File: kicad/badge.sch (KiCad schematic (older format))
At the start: 11 parts, among them SW1 SPST

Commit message: wire pin 20 and 21 to +5v
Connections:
- net +5V: now also IC?.20 (AVCC), IC?.21 (AREF)
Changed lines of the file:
@@
 	8200 2650 8200 3150
 Connection ~ 8200 3150
+Wire Wire Line
+	4550 2650 4550 3250
+Wire Wire Line
+	4550 3250 4700 3250
+Connection ~ 4550 2650
+Wire Wire Line
+	4700 2950 4550 2950
+Connection ~ 4550 2950
 $EndSCHEMATC

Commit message: 9v battery connector
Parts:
- added P?: 9v battery, symbol CONN_01X02
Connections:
- net GND: now also P?.1 (P1)
- net VCC: now also P?.2 (P2)
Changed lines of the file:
@@
 	4700 2950 4550 2950
 Connection ~ 4550 2950
+$Comp
+L CONN_01X02 P?
+U 1 1 58E1B172
+P 2450 1000
+F 0 "P?" H 2450 1150 50  0000 C CNN
+F 1 "9v battery " V 2550 1000 50  0000 C CNN
+F 2 "" H 2450 1000 50  0000 C CNN
+F 3 "" H 2450 1000 50  0000 C CNN
+	1    2450 1000
+	-1   0    0    1
+$EndComp
+$Comp
+L VCC #PWR?
+U 1 1 58E1B2A6
+P 3000 900
+F 0 "#PWR?" H 3000 750 50  0001 C CNN
+F 1 "VCC" H 3000 1050 50  0000 C CNN
+F 2 "" H 3000 900 50  0000 C CNN
+F 3 "" H 3000 900 50  0000 C CNN
+	1    3000 900
+	1    0    0    -1
+$EndComp
+$Comp
+L GND #PWR?
+U 1 1 58E1B2D2
+P 3000 1200
+F 0 "#PWR?" H 3000 950 50  0001 C CNN
+F 1 "GND" H 3000 1050 50  0000 C CNN
+F 2 "" H 3000 1200 50  0000 C CNN
+F 3 "" H 3000 1200 50  0000 C CNN
+	1    3000 1200
+	1    0    0    -1
+$EndComp
+Wire Wire Line
+	2650 950  3000 950
+Wire Wire Line
+	3000 950  3000 900
+Wire Wire Line
+	2650 1050 3000 1050
+Wire Wire Line
+	3000 1050 3000 1200
 $EndSCHEMATC

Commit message: FTDI programmer connection pins
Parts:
- added P?: FTDI programmer, symbol CONN_01X06
- C?: value C -> 0.1uF
- C?: value C -> 0x33uF
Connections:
- net +5V: now also P?.5 (P5)
- net at IC?.1 ((PCINT14/~RESET~)PC6): now also P?.1 (P1)
- net at IC?.2 ((PCINT16/RXD)PD0): now also P?.2 (P2)
- net at IC?.3 ((PCINT17/TXD)PD1): now also P?.3 (P3)
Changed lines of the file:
@@
 P 2600 1950
 F 0 "C?" H 2625 2050 50  0000 L CNN
-F 1 "C" H 2625 1850 50  0000 L CNN
+F 1 "0.1uF" H 2625 1850 50  0000 L CNN
 F 2 "" H 2638 1800 50  0000 C CNN
 F 3 "" H 2600 1950 50  0000 C CNN
@@
 P 1300 2000
 F 0 "C?" H 1325 2100 50  0000 L CNN
-F 1 "C" H 1325 1900 50  0000 L CNN
+F 1 "0x33uF" H 1325 1900 50  0000 L CNN
 F 2 "" H 1338 1850 50  0000 C CNN
 F 3 "" H 1300 2000 50  0000 C CNN
@@
 Wire Wire Line
 	3000 1050 3000 1200
+$Comp
+L CONN_01X06 P?
+U 1 1 58E1B8C9
+P 7550 4350
+F 0 "P?" H 7550 4700 50  0000 C CNN
+F 1 "FTDI programmer" V 7650 4350 50  0000 C CNN
+F 2 "" H 7550 4350 50  0000 C CNN
+F 3 "" H 7550 4350 50  0000 C CNN
+	1    7550 4350
+	1    0    0    -1
+$EndComp
+$Comp
+L GND #PWR?
+U 1 1 58E1B9A0
+P 7250 4750
+F 0 "#PWR?" H 7250 4500 50  0001 C CNN
+F 1 "GND" H 7250 4600 50  0000 C CNN
+F 2 "" H 7250 4750 50  0000 C CNN
+F 3 "" H 7250 4750 50  0000 C CNN
+	1    7250 4750
+	1    0    0    -1
+$EndComp
+Wire Wire Line
+	7400 4600 7250 4600
+Wire Wire Line
+	7250 4600 7250 4750
+Wire Wire Line
+	6600 4100 7350 4100
+Wire Wire Line
+	6600 4250 6750 4250
+Wire Wire Line
+	6750 4250 6750 4200
+Wire Wire Line
+	6750 4200 7350 4200
+Wire Wire Line
+	6600 4350 7150 4350
+Wire Wire Line
+	7150 4350 7150 4300
+Wire Wire Line
+	7150 4300 7350 4300
+$Comp
+L +5V #PWR?
+U 1 1 58E1BF97
+P 7000 4750
+F 0 "#PWR?" H 7000 4600 50  0001 C CNN
+F 1 "+5V" H 7000 4890 50  0000 C CNN
+F 2 "" H 7000 4750 50  0000 C CNN
+F 3 "" H 7000 4750 50  0000 C CNN
+	1    7000 4750
+	-1   0    0    1
+$EndComp
+Wire Wire Line
+	7000 4500 7000 4750
+Wire Wire Line
+	7000 4500 7350 4500
 $EndSCHEMATC

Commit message: fix value and reference componentc fields
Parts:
- removed 16Mhz1: Crystal, symbol Crystal
- removed 22pF2: C, symbol C
- removed R1: R, symbol R
- added C?: 22pF, symbol C
- added Y?: 16Mhz, symbol Crystal
- C?: renamed from 22pF1; value C -> 22pF
- C?: renamed from 10uF1; value C -> 10uF
- R?: renamed from 10k1; value R -> 10k
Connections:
- net GND: now also C?.1
- net at C?.2, IC?.9 ((PCINT6/XTAL1/TOSC1)PB6): now also Y?.1
- net at IC?.10 ((PCINT7/XTAL2/TOSC2)PB7): now also C?.2, Y?.2
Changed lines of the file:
@@
 $EndDescr
-$Comp
-L R R1
-U 1 1 58E158FB
-P 6100 3850
-F 0 "R1" V 6180 3850 50  0000 C CNN
-F 1 "R" V 6100 3850 50  0000 C CNN
-F 2 "" V 6030 3850 50  0000 C CNN
-F 3 "" H 6100 3850 50  0000 C CNN
-	1    6100 3850
-	1    0    0    -1
-$EndComp
 $Comp
 L GND #PWR01
@@
 $EndComp
 $Comp
-L R 10k1
+L R R?
 U 1 1 58E15AC1
 P 7450 2250
-F 0 "10k1" V 7530 2250 50  0000 C CNN
-F 1 "R" V 7450 2250 50  0000 C CNN
+F 0 "R?" V 7530 2250 50  0000 C CNN
+F 1 "10k" V 7450 2250 50  0000 C CNN
 F 2 "" V 7380 2250 50  0000 C CNN
 F 3 "" H 7450 2250 50  0000 C CNN
@@
 $EndComp
 $Comp
-L Crystal 16Mhz1
-U 1 1 58E15B48
-P 7350 3350
-F 0 "16Mhz1" H 7350 3500 50  0000 C CNN
-F 1 "Crystal" H 7350 3200 50  0000 C CNN
-F 2 "" H 7350 3350 50  0000 C CNN
-F 3 "" H 7350 3350 50  0000 C CNN
-	1    7350 3350
-	0    1    1    0
-$EndComp
-$Comp
-L C 22pF1
+L C C?
 U 1 1 58E15B8A
 P 7700 3100
-F 0 "22pF1" H 7725 3200 50  0000 L CNN
-F 1 "C" H 7725 3000 50  0000 L CNN
+F 0 "C?" H 7725 3200 50  0000 L CNN
+F 1 "22pF" H 7725 3000 50  0000 L CNN
 F 2 "" H 7738 2950 50  0000 C CNN
 F 3 "" H 7700 3100 50  0000 C CNN
 	1    7700 3100
-	0    1    1    0
-$EndComp
-$Comp
-L C 22pF2
-U 1 1 58E15BB3
-P 7750 3650
-F 0 "22pF2" H 7775 3750 50  0000 L CNN
-F 1 "C" H 7775 3550 50  0000 L CNN
-F 2 "" H 7788 3500 50  0000 C CNN
-F 3 "" H 7750 3650 50  0000 C CNN
-	1    7750 3650
 	0    1    1    0
 $EndComp
@@
 $EndComp
 $Comp
-L C 10uF1
+L C C?
 U 1 1 58E164D8
 P 4150 2800
-F 0 "10uF1" H 4175 2900 50  0000 L CNN
-F 1 "C" H 4175 2700 50  0000 L CNN
+F 0 "C?" H 4175 2900 50  0000 L CNN
+F 1 "10uF" H 4175 2700 50  0000 L CNN
 F 2 "" H 4188 2650 50  0000 C CNN
 F 3 "" H 4150 2800 50  0000 C CNN
@@
 $EndComp
 Wire Wire Line
-	6800 3100 7550 3100
+	6800 3100 7350 3100
+Wire Wire Line
+	7350 3100 7550 3100
 Wire Wire Line
 	7350 3200 7350 3100
@@
 	7350 3500 7350 3650
 Wire Wire Line
-	6800 3650 7600 3650
+	6800 3650 7350 3650
+Wire Wire Line
+	7350 3650 7600 3650
 Wire Wire Line
 	7850 3100 8200 3100
 Wire Wire Line
-	8200 3100 8200 3800
+	8200 3100 8200 3150
+Wire Wire Line
+	8200 3150 8200 3650
+Wire Wire Line
+	8200 3650 8200 3800
 Wire Wire Line
 	7900 3650 8200 3650
@@
 	4700 4850 4450 4850
 Wire Wire Line
-	4150 2650 4700 2650
+	4150 2650 4550 2650
+Wire Wire Line
+	4550 2650 4700 2650
 Wire Wire Line
 	4150 2650 4150 2250
@@
 	4150 2950 4150 3100
 Wire Wire Line
-	6600 2650 6950 2650
+	6600 2650 6850 2650
+Wire Wire Line
+	6850 2650 6950 2650
 Wire Wire Line
 	7300 2250 6850 2250
@@
 	7900 2250 7600 2250
 Wire Wire Line
-	1300 1750 1600 1750
+	1300 1750 1500 1750
+Wire Wire Line
+	1500 1750 1600 1750
 Wire Wire Line
 	1300 1750 1300 1850
 Wire Wire Line
-	2000 2050 2000 2350
+	2000 2050 2000 2250
+Wire Wire Line
+	2000 2250 2000 2350
 Wire Wire Line
 	1300 2150 1300 2250
 Wire Wire Line
-	1300 2250 2600 2250
+	1300 2250 2000 2250
+Wire Wire Line
+	2000 2250 2600 2250
 Connection ~ 2000 2250
 Wire Wire Line
 	2600 2250 2600 2100
 Wire Wire Line
-	2400 1750 3100 1750
+	2400 1750 2600 1750
+Wire Wire Line
+	2600 1750 3100 1750
 Wire Wire Line
 	2600 1750 2600 1800
@@
 Connection ~ 7350 3650
 Wire Wire Line
-	4450 4850 4450 5150
+	4450 4850 4450 4950
+Wire Wire Line
+	4450 4950 4450 5150
 Wire Wire Line
 	7950 2650 8200 2650
@@
 Connection ~ 8200 3150
 Wire Wire Line
-	4550 2650 4550 3250
+	4550 2650 4550 2950
+Wire Wire Line
+	4550 2950 4550 3250
 Wire Wire Line
 	4550 3250 4700 3250
@@
 Wire Wire Line
 	7000 4500 7350 4500
+$Comp
+L Crystal Y?
+U 1 1 58E1C7EA
+P 7350 3350
+F 0 "Y?" H 7350 3500 50  0000 C CNN
+F 1 "16Mhz" H 7350 3200 50  0000 C CNN
+F 2 "" H 7350 3350 50  0000 C CNN
+F 3 "" H 7350 3350 50  0000 C CNN
+	1    7350 3350
+	0    1    1    0
+$EndComp
+$Comp
+L C C?
+U 1 1 58E1C898
+P 7750 3650
+F 0 "C?" H 7775 3750 50  0000 L CNN
+F 1 "22pF" H 7775 3550 50  0000 L CNN
+F 2 "" H 7788 3500 50  0000 C CNN
+F 3 "" H 7750 3650 50  0000 C CNN
+	1    7750 3650
+	0    1    1    0
+$EndComp
 $EndSCHEMATC

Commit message: fix value: 33uF -> 0.33uF
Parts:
- C?: value 0x33uF -> 0.33uF
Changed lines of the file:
@@
 P 1300 2000
 F 0 "C?" H 1325 2100 50  0000 L CNN
-F 1 "0x33uF" H 1325 1900 50  0000 L CNN
+F 1 "0.33uF" H 1325 1900 50  0000 L CNN
 F 2 "" H 1338 1850 50  0000 C CNN
 F 3 "" H 1300 2000 50  0000 C CNN

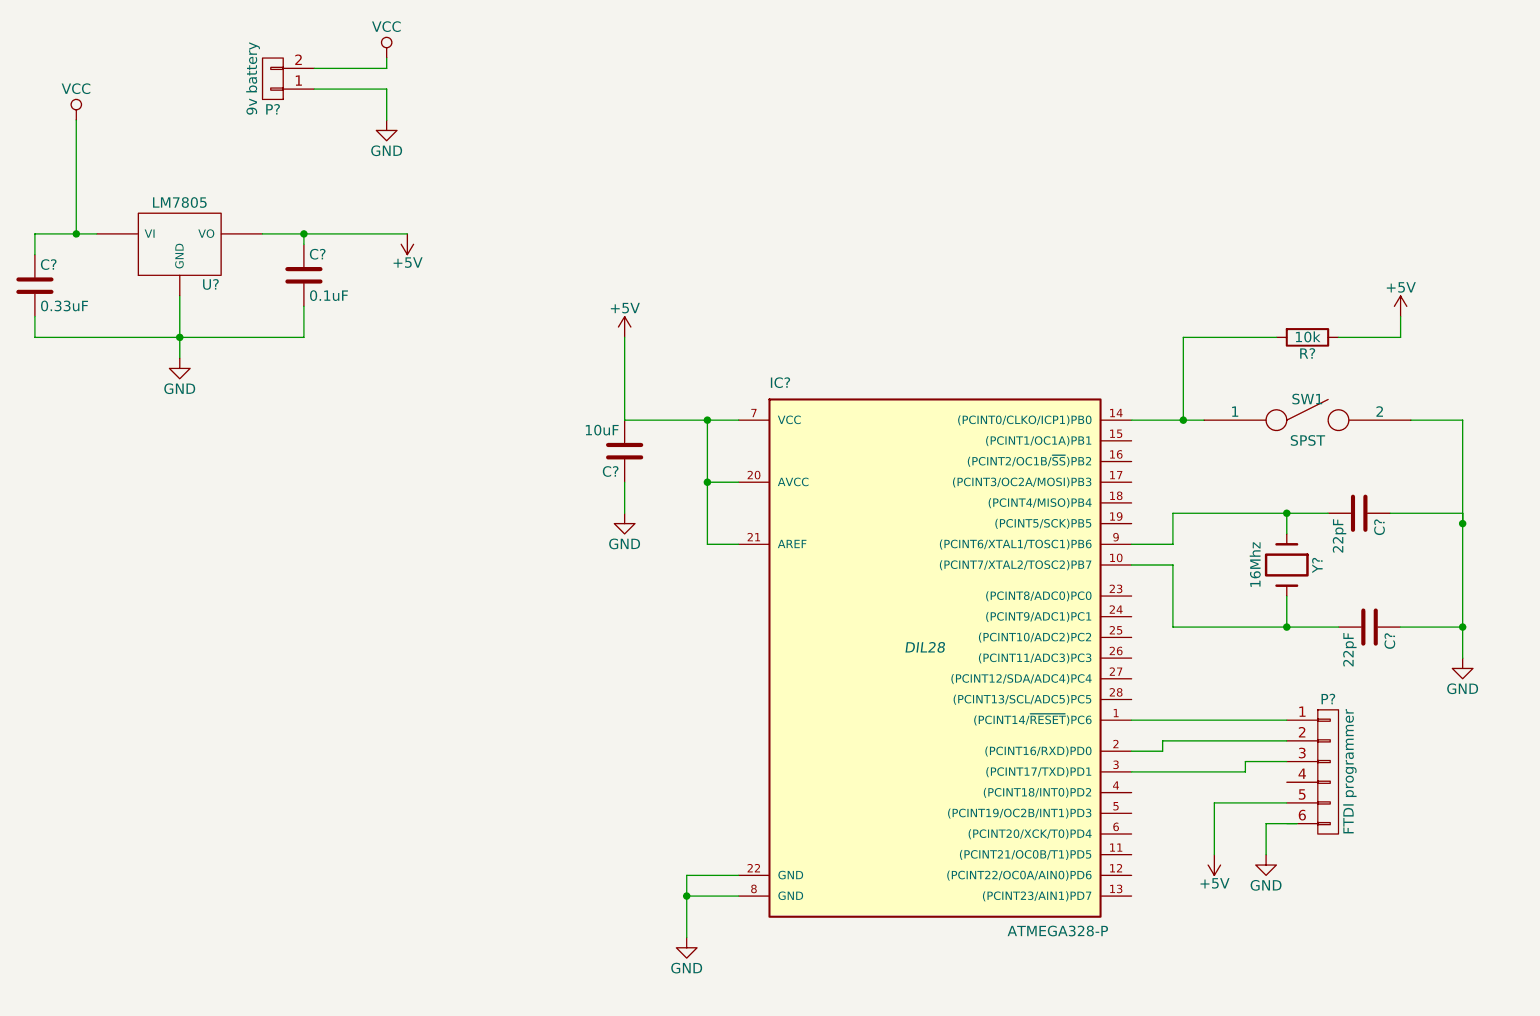
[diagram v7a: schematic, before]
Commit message: fix ftdi connector trace
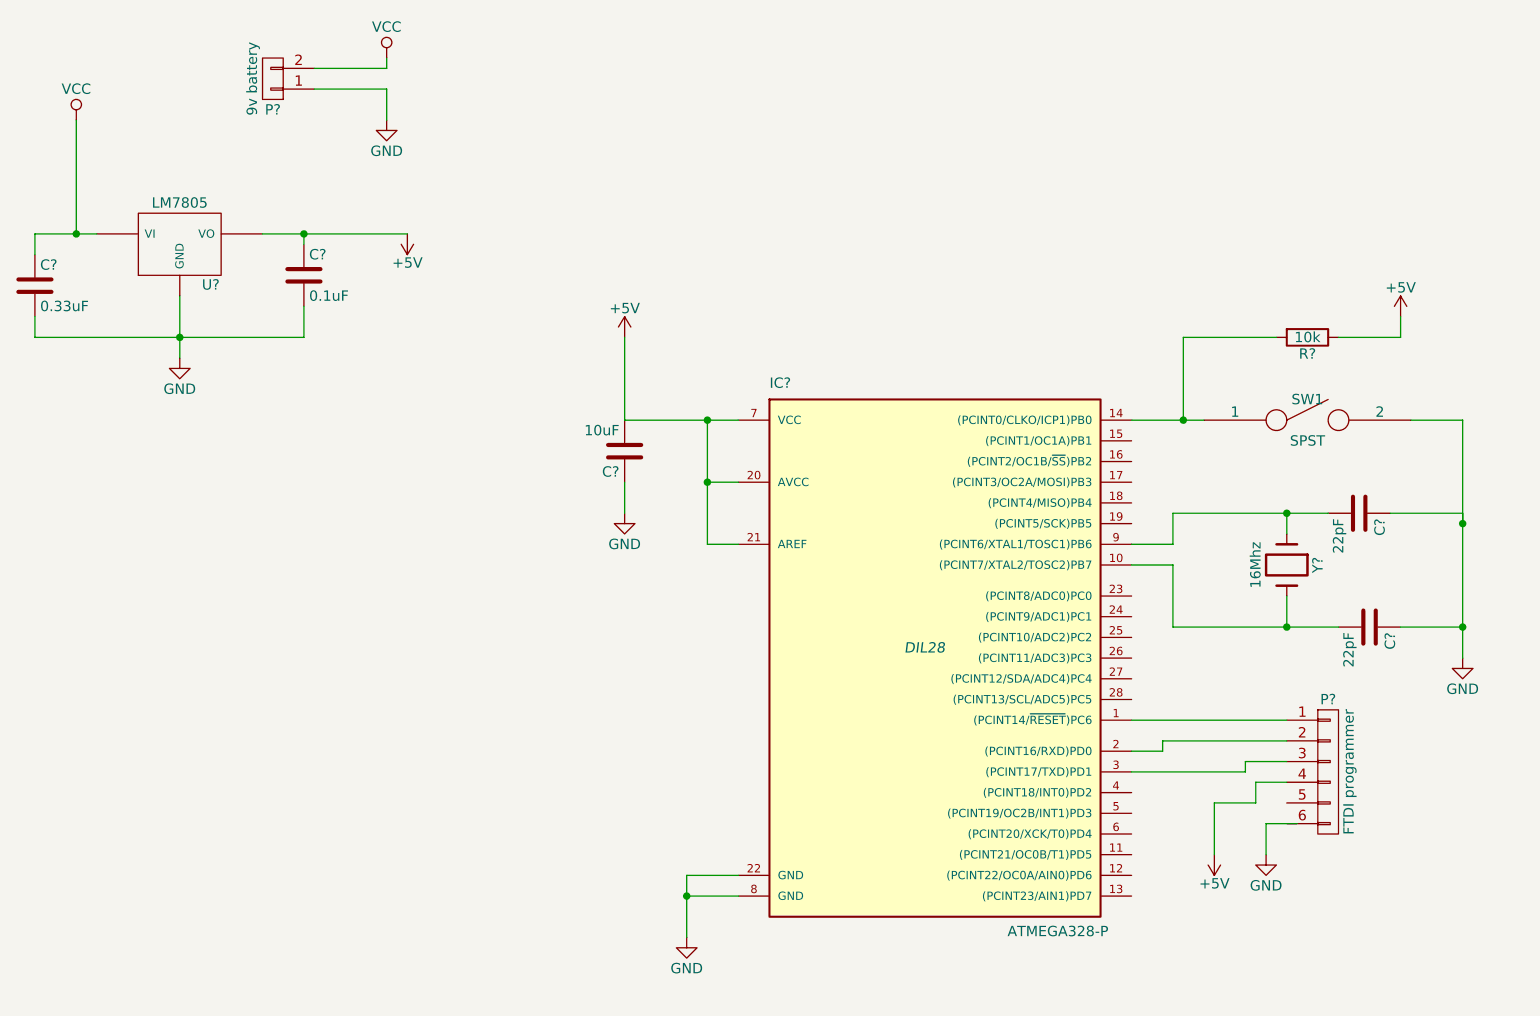
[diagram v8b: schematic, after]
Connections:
- net +5V: now also P?.4 (P4); no longer P?.5 (P5)
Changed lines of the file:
@@
 $EndComp
 Wire Wire Line
-	6800 3100 7350 3100
-Wire Wire Line
-	7350 3100 7550 3100
+	6800 3100 7550 3100
 Wire Wire Line
 	7350 3200 7350 3100
@@
 	7350 3500 7350 3650
 Wire Wire Line
-	6800 3650 7350 3650
-Wire Wire Line
-	7350 3650 7600 3650
+	6800 3650 7600 3650
 Wire Wire Line
 	7850 3100 8200 3100
 Wire Wire Line
-	8200 3100 8200 3150
-Wire Wire Line
-	8200 3150 8200 3650
-Wire Wire Line
-	8200 3650 8200 3800
+	8200 3100 8200 3800
 Wire Wire Line
 	7900 3650 8200 3650
@@
 	4700 4850 4450 4850
 Wire Wire Line
-	4150 2650 4550 2650
-Wire Wire Line
-	4550 2650 4700 2650
+	4150 2650 4700 2650
 Wire Wire Line
 	4150 2650 4150 2250
@@
 	4150 2950 4150 3100
 Wire Wire Line
-	6600 2650 6850 2650
-Wire Wire Line
-	6850 2650 6950 2650
+	6600 2650 6950 2650
 Wire Wire Line
 	7300 2250 6850 2250
@@
 	7900 2250 7600 2250
 Wire Wire Line
-	1300 1750 1500 1750
-Wire Wire Line
-	1500 1750 1600 1750
+	1300 1750 1600 1750
 Wire Wire Line
 	1300 1750 1300 1850
 Wire Wire Line
-	2000 2050 2000 2250
-Wire Wire Line
-	2000 2250 2000 2350
+	2000 2050 2000 2350
 Wire Wire Line
 	1300 2150 1300 2250
 Wire Wire Line
-	1300 2250 2000 2250
-Wire Wire Line
-	2000 2250 2600 2250
+	1300 2250 2600 2250
 Connection ~ 2000 2250
 Wire Wire Line
 	2600 2250 2600 2100
 Wire Wire Line
-	2400 1750 2600 1750
-Wire Wire Line
-	2600 1750 3100 1750
+	2400 1750 3100 1750
 Wire Wire Line
 	2600 1750 2600 1800
@@
 Connection ~ 7350 3650
 Wire Wire Line
-	4450 4850 4450 4950
-Wire Wire Line
-	4450 4950 4450 5150
+	4450 4850 4450 5150
 Wire Wire Line
 	7950 2650 8200 2650
@@
 Connection ~ 8200 3150
 Wire Wire Line
-	4550 2650 4550 2950
-Wire Wire Line
-	4550 2950 4550 3250
+	4550 2650 4550 3250
 Wire Wire Line
 	4550 3250 4700 3250
@@
 Wire Wire Line
 	7000 4500 7000 4750
-Wire Wire Line
-	7000 4500 7350 4500
 $Comp
 L Crystal Y?
@@
 	0    1    1    0
 $EndComp
+Wire Wire Line
+	7200 4400 7350 4400
+Wire Wire Line
+	7200 4400 7200 4500
+Wire Wire Line
+	7200 4500 7000 4500
 $EndSCHEMATC
